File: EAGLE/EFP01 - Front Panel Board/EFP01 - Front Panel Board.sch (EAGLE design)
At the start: 109 parts, among them J20 Intel EDISON, J21 PWRBUTTON, J22 SERIAL CONS., J23 B14B-PH, J3 USB-A, J4 101-00581-59, J9 ESTOP, Q2 25MHz, U10 FT231XS-R, U11 74LVC1T45, U12 74LVC1T45, U13 74LVC1T45, U14 74LVC1T45, U15 74LVC1T45, U16 TXS0206-29, U17 74LVC, U18 MIC2026-1YM, U19 MIC2026-1YM, U20 74LVC, U21 74LVC1T45, U22 74LVC1T45, U3 93LC66A, U4 LAN9514, U9 SP3485

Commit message: Finalized schematics (minus potential LDO regulator) for all boards. Layout partially done for EFD01
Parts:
- removed C36: 220uF, TinWhiskers:CPL-CAP-ALU-SMD-220-50V
- removed C50: 470uF, TinWhiskers:CPL-CAP-ALU-SMD-470UF-25V
- removed FID4, FID5, FID6: FIDUCIAL, FirePick:FIDUCIAL
- removed J21: PWRBUTTON, TinWhiskers:CPL-CON-HEADER-0.1IN-2P-M
- removed J22: SERIAL CONS., TinWhiskers:CPL-CON-HEADER-0.1IN-4P-M
- removed J23: B14B-PH, TinWhiskers:CPL-CON-JST-2.0MM-14P-M-VRT
- removed J9: ESTOP, TinWhiskers:CPL-CON-HEADER-0.1IN-2P-M
- removed L2: 100uH, TinWhiskers:CPL-IND-100UH-1.8A
- added C1: 220uF, TinWhiskers:CPL-CAP-ALU-SMD-220UF-16V
- added C3: 470uF, TinWhiskers:CPL-CAP-ALU-SMD-470UF-10V
- added J1: PWRBTN, TinWhiskers:CPL-CON-JST-2.0MM-4P-M-SMT-RA
- added J16, J17, J6: S8B-PH-SM4, TinWhiskers:CPL-CON-JST-2.0MM-8P-M-RA
- added J18: S6B-PH-SM4, TinWhiskers:CPL-CON-JST-2.0MM-6P-M-RA
- added J2: ESTOP, TinWhiskers:CPL-CON-JST-2.0MM-2P-M-SMT-RA
- added J5: LCD, TinWhiskers:CPL-CON-HEADER-0.1IN-17P2-M
- added J7: USB-B, TinWhiskers:CPL-CON-USB-B-SMT-VERT
- added L1: 100uH, TinWhiskers:CPL-IND-100UH-700MA-2020
- added R1: 4.7K, TinWhiskers:CPL-RES-0603-4.7K-0.1W
- added R2: 10K, TinWhiskers:CPL-RES-0603-10K-0.1W
- added R3: ORNG, TinWhiskers:CPL-RES-0603-0-0.1W
- added TB1: DCIN, TinWhiskers:CPL-TBLK-SCR-3CKT-5.0MM-OST
- added U1, U2, U23, U24, U25, U26, U27, U28, U30, U5, U6, U7, U8: 74LVC1T45, TinWhiskers:CPL-TRS-74LVC1T45
- J3: value USB-A -> USB-A(2.0); device TinWhiskers:CPL-CON-HEADER-0.1IN-4P-M -> TinWhiskers:CPL-CON-USB-A-THRU-VERT-2.0; PARTNO 68000-104HLF -> (none)
- U17, U20: value 74LVC -> OR
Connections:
- removed net ESTOP_OE: J9.2
- new net !ENBL_MOD: J16.2, J17.2, J18.2, J6.2
- new net +24V: J16.1, J17.1, J18.1, J6.1, R3.2, TB1.1
- new net 74DIR: J20.GP165, U30.3
- new net 74DIRO: U1.5, U2.5, U23.5, U24.5, U25.5, U26.5, U27.5, U28.5, U30.4, U5.5, U6.5, U7.5, U8.5
- new net D0O: J20.GP40, U24.4
- new net D1O: J20.GP41, U23.4
- new net D2O: J20.GP42, U7.4
- new net D3O: J20.GP43, U8.4
- new net D4O: J20.GP44, U6.4
- new net D5O: J20.GP45, U5.4
- new net D6O: J20.GP46, U1.4
- new net D7O: J20.GP47, U2.4
- new net ESTOPIN: J2.1, R2.1
- new net LCD_BL: J5.23
- new net LCD_CLK: J5.34
- new net LCD_D10: J5.16
- new net LCD_D11: J5.17
- new net LCD_D12: J5.18
- new net LCD_D13: J5.19
- new net LCD_D14: J5.20
- new net LCD_D15: J5.21
- new net LCD_D8: J5.14
- new net LCD_D9: J5.15
- new net LCD_FCS: J5.32
- new net LCD_MISO: J5.29
- new net LCD_MOSI: J5.30
- new net LCD_PEN: J5.31
- new net LCD_RST: J5.5
- new net LCD_SDCS: J5.22
- new net LCD_TCS: J5.33
- new net LCSO: J20.GP183, U25.4
- new net LRDO: J20.GP182, U27.4
- new net LRSO: J20.GP49, U28.4
- new net LWRO: J20.GP48, U26.4
- new net N$10: J2.2, R1.2
- new net NC: J5.28
- new net VDD: J5.24, J5.25
- net !PWRBTN: now also J1.1; no longer J21.1
- net +1V8: now also U1.1, U2.6, U23.1, U24.1, U25.6, U26.6, U27.6, U28.6, U30.6, U5.1, U6.1, U7.1, U8.6
- net +3V3: now also C3.POS, L1.2, R2.2, U1.6, U2.1, U23.6, U24.6, U25.1, U26.1, U27.1, U28.1, U30.1, U5.6, U6.6, U7.6, U8.1; no longer C50.POS, J23.1, L2.2
- net +5V: now also C1.POS, J18.6, J6.6, TB1.2; no longer C36.POS
- net A: now also J16.4, J17.4, J18.4, J6.4
- net B: now also J16.5, J17.5, J18.5, J6.5
- net DM: now also J7.3; no longer J22.3
- net DP: now also J7.2; no longer J22.2
- net EE_D+: now also J16.7
- net EE_D-: now also J16.8
- net GND: now also C1.NEG, C3.NEG, J1.2, J1.4, J16.3, J17.3, J18.3, J3.GND, J5.26, J5.27, J6.3, J7.4, R1.1, TB1.3, U1.2, U2.2, U23.2, U24.2, U25.2, U26.2, U27.2, U28.2, U30.2, U30.5, U5.2, U6.2, U7.2, U8.2; no longer C36.NEG, C50.NEG, J21.2, J22.4, J23.2, J3.4
- net LCD_CS: now also J5.1, U25.3; no longer J20.GP183, J23.11
- net LCD_D0: now also J5.6, U24.3; no longer J20.GP40, J23.3
- net LCD_D1: now also J5.7, U23.3; no longer J20.GP41, J23.4
- net LCD_D2: now also J5.8, U7.3; no longer J20.GP42, J23.5
- net LCD_D3: now also J5.9, U8.3; no longer J20.GP43, J23.6
- net LCD_D4: now also J5.10, U6.3; no longer J20.GP44, J23.7
- net LCD_D5: now also J5.11, U5.3; no longer J20.GP45, J23.8
- net LCD_D6: now also J5.12, U1.3; no longer J20.GP46, J23.9
- net LCD_D7: now also J5.13, U2.3; no longer J20.GP47, J23.10
- net LCD_RD: now also J5.4, U27.3; no longer J20.GP182, J23.14
- net LCD_RS: now also J5.2, U28.3; no longer J20.GP49, J23.12
- net LCD_WR: now also J5.3, U26.3; no longer J20.GP48, J23.13
- net N$16: now also L1.1; no longer L2.1
- net N$2: now also J7.1; no longer J22.1
- net N$5: now also J1.3, R3.1; no longer J9.1
- net PWR1: now also J16.6
- net PWR2: now also J17.6
- net PWR3: now also J3.VCC; no longer J3.1
- net ULC_D+: now also J17.7
- net ULC_D-: now also J17.8
- net USBA_D+: now also J3.D+; no longer J3.3
- net USBA_D-: now also J3.D-; no longer J3.2
- net USBMCU+: now also J6.7
- net USBMCU-: now also J6.8
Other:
- note added: "CAMERA"
- note added: "DC IN"
- note added: "EFFECTOR"
- note added: "EMC03 CONNX"
- note added: "END"
- note added: "IC PWR"
- note added: "MOD."
- note added: "TEST PADS"
- note added: "TOOL1"
- note added: "UP-LOOK"
- note added: "USB CHIP (S CONS)"
- note removed: "Change to SMD pads, bottom"
- note removed: "EMERGENCY STOP SWITCH (NORMALLY CLOSED TYPE) USE JUMPER IF NOT PRESENT"
- note removed: "LOGIC IC PWR"
- note removed: "TEST POINTS"
- note removed: "TODO: CHANGE J3 TO VERT. MOUNT USB "A" CONNECTOR"
- note removed: "TODO: Replace with 34-pin 2-row 0.1" rect."
- note removed: "USB-A CHIP (S CONS)"
- note removed: "VDD"
- note removed: "VSS"
- moved on the sheet: C13, C14, C18, C19, C2, C20, C21, C22, C23, C24, C25, C26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

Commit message: Routed all boards. EFP01 has a serious problem with spacing. Even on minimum allowable there are 300 DRC errors.
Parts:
- removed C1: 220uF, TinWhiskers:CPL-CAP-ALU-SMD-220UF-16V
- removed C33, C34, C35: 0.1uF, TinWhiskers:CPL-CAP-X5R-0603-0.1UF-35V
- removed C51: 0.47uF, TinWhiskers:CPL-CAP-X7R-0603-0.47UF-10V
- removed D15: SJPB-H6, TinWhiskers:CPL-DIO-SJPB-H6-SM2
- removed J4: 101-00581-59, TinWhiskers:CPL-CON-MICSROSD(SD)-CD
- removed L1: 100uH, TinWhiskers:CPL-IND-100UH-700MA-2020
- removed R17, R23: 10.5K, TinWhiskers:CPL-RES-0603-10.5K-0.1W
- removed U16: TXS0206-29, TinWhiskers:TXS0206-29
- removed VR2: SI-8033JD, TinWhiskers:CPL-REG-SWI-3.3V-1.5A
- added C4: 10uF, TinWhiskers:CPL-CAP-ALU-6.4MM-10UF-10V
- added VR1: LMS8117AMP-3.3/NOPB, TinWhiskers:CPL-REG-LIN-3.3V-1A
- C3: value 470uF -> 10uF; device TinWhiskers:CPL-CAP-ALU-SMD-470UF-10V -> TinWhiskers:CPL-CAP-ALU-6.4MM-10UF-10V
- J5: device TinWhiskers:CPL-CON-HEADER-0.1IN-17P2-M -> TinWhiskers:CPL-CON-LCD-HDR-0.1IN-17P2-F
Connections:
- removed net CLKA: J20.GP78, U16.CLKA
- removed net CLKB: J4.CLK, U16.CLKB
- removed net CLKF: J20.GP84, U16.CLKF
- removed net CMD: J4.CMD
- removed net CMDA: J20.GP79, U16.CMDA
- removed net CMDB: U16.CMDB
- removed net DAT0A: J20.GP80, U16.DAT0A
- removed net DAT0B: J4.DAT0, U16.DAT0B
- removed net DAT1A: J20.GP81, U16.DAT1A
- removed net DAT1B: J4.DAT1, U16.DAT1B
- removed net DAT2: J4.DAT2
- removed net DAT2A: J20.GP82, U16.DAT2A
- removed net DAT2B: U16.DAT2B
- removed net DAT3: J4.CD/DAT3
- removed net DAT3A: J20.GP83, U16.DAT3A
- removed net DAT3B: U16.DAT3B
- removed net EN: R17.1, U16.EN
- removed net N$16: D15.C, L1.1, VR2.2
- removed net N$17: C51.2, VR2.5
- removed net SD_CD: J20.GP77, J4.CD, R23.1, U16.CD
- removed net VCCB: C34.2, J4.VDD, U16.VCCB
- new net RESET: U10.!RESET
- net !RXLED: now also U10.CBUS2
- net !TXLED: now also U10.CBUS1
- net +1V8: no longer C35.2, R17.2, R23.2, U16.VCCA
- net +3V3: now also C4.POS, U10.VCCIO, VR1.OUT; no longer C3.POS, C33.2, L1.2, U16.VBATT, VR2.4
- net +5V: now also C3.POS, VR1.IN; no longer C1.POS, VR2.1
- net DM: now also U10.USBDM
- net DP: now also U10.USBDP
- net GND: now also C4.NEG, RJ1.GND, U10.GND@16, U10.GND@6, VR1.GND, VR1.TAB; no longer C1.NEG, C33.1, C34.1, C35.1, C51.1, D15.A, J4.GND, J4.GND2, J4.NC, J4.VSS, U16.GND@C2, U16.GND@C3, VR2.3, VR2.GND
- net N$1: now also U10.3V3OUT
- net RXD: now also U10.RXD
- net TXDO: now also U10.TXD
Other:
- note added: "VOLTAGE REG"
- note removed: "* 5V Switching Regulator: Powers LEDs, Endstops"
- note removed: "MICRO SD INTERFACE"
- note removed: "TODO: MAY CHANGE TO FULL-SIZE SD?"
- moved on the sheet: C3, J5

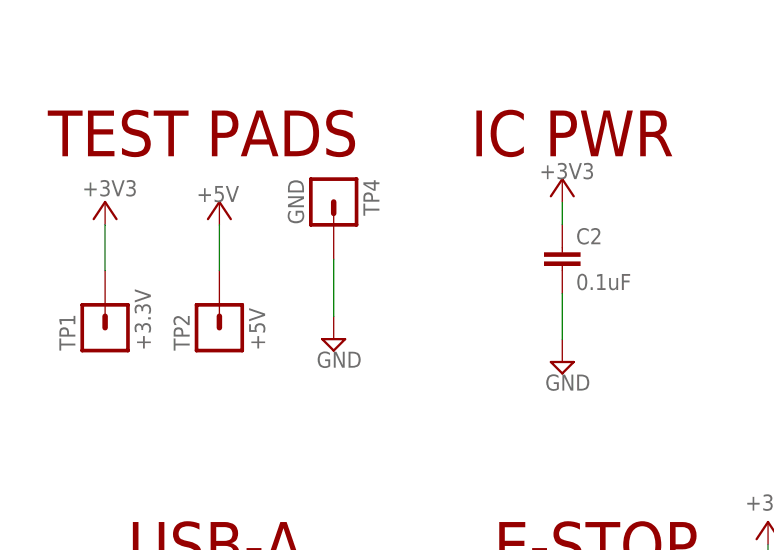
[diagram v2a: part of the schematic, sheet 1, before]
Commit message: Completed boards. Please look at airwires connecting thermal pads to GND vias. They shouldn't be present due to the vias.
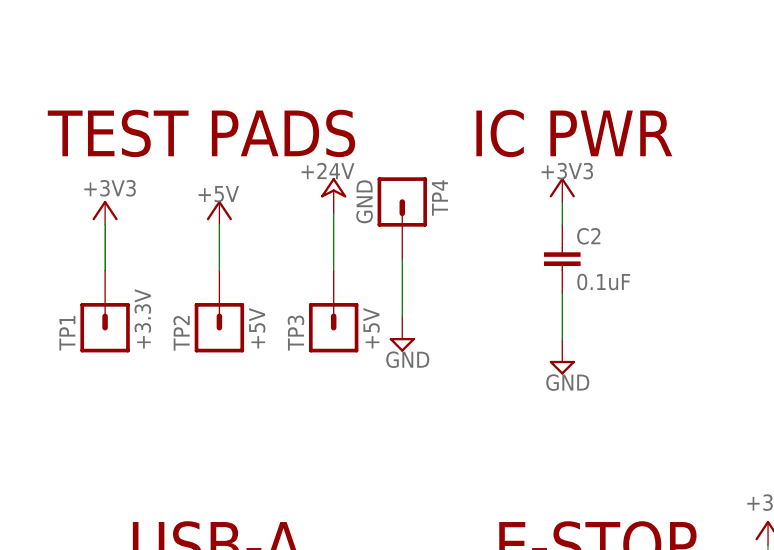
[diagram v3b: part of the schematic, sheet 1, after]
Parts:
- added TP3: +5V, TinWhiskers:TPAD
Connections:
- net +24V: now also TP3.2
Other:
- moved on the sheet: TP4
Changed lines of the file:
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@@
 <part name="+3V32" library="supply1" deviceset="+3V3" device=""/>
 <part name="SUPPLY45" library="TinWhiskers" deviceset="GND" device=""/>
+<part name="TP3" library="TinWhiskers" deviceset="TPAD" device="" value="+5V">
+<attribute name="DNP" value="T"/>
+<attribute name="PARTNO" value="N/A"/>
+</part>
+<part name="P+8" library="supply1" deviceset="+24V" device=""/>
 </parts>
 <sheets>
@@
 <instance part="SUPPLY82" gate="GND" x="243.84" y="116.84"/>
 <instance part="SUPPLY83" gate="GND" x="218.44" y="116.84"/>
-<instance part="TP4" gate="G$1" x="40.64" y="232.41" rot="R270">
-<attribute name="DNP" x="40.64" y="232.41" size="1.778" layer="96" rot="R270" display="off"/>
-<attribute name="PARTNO" x="40.64" y="232.41" size="1.778" layer="96" display="off"/>
+<instance part="TP4" gate="G$1" x="48.26" y="232.41" rot="R270">
+<attribute name="DNP" x="48.26" y="232.41" size="1.778" layer="96" rot="R270" display="off"/>
+<attribute name="PARTNO" x="48.26" y="232.41" size="1.778" layer="96" display="off"/>
 </instance>
 <instance part="TP2" gate="G$1" x="27.94" y="226.06" rot="R90">
@@
 <attribute name="VALUE" x="12.7" y="236.855" size="1.778" layer="96"/>
 </instance>
-<instance part="SUPPLY49" gate="GND" x="40.64" y="220.98"/>
+<instance part="SUPPLY49" gate="GND" x="48.26" y="220.98"/>
 <instance part="R1" gate="G$1" x="81.28" y="172.72" rot="R90"/>
 <instance part="SUPPLY3" gate="GND" x="81.28" y="162.56"/>
@@
 <instance part="+3V32" gate="G$1" x="114.3" y="81.28" smashed="yes">
 <attribute name="VALUE" x="111.76" y="81.915" size="1.778" layer="96"/>
+</instance>
+<instance part="TP3" gate="G$1" x="40.64" y="226.06" rot="R90">
+<attribute name="DNP" x="40.64" y="226.06" size="1.778" layer="96" rot="R90" display="off"/>
+<attribute name="PARTNO" x="40.64" y="226.06" size="1.778" layer="96" display="off"/>
+</instance>
+<instance part="P+8" gate="1" x="40.64" y="237.49" smashed="yes">
+<attribute name="VALUE" x="36.83" y="238.76" size="1.778" layer="96"/>
 </instance>
 </instances>
@@
 <segment>
 <pinref part="TP4" gate="G$1" pin="2"/>
-<wire x1="40.64" y1="229.87" x2="40.64" y2="223.52" width="0.1524" layer="91"/>
+<wire x1="48.26" y1="229.87" x2="48.26" y2="223.52" width="0.1524" layer="91"/>
 <pinref part="SUPPLY49" gate="GND" pin="GND"/>
 </segment>
@@
 <pinref part="P+13" gate="1" pin="+24V"/>
 </segment>
-</net>
+<segment>
+<pinref part="TP3" gate="G$1" pin="2"/>
+<wire x1="40.64" y1="228.6" x2="40.64" y2="234.95" width="0.1524" layer="91"/>
+<pinref part="P+8" gate="1" pin="+24V"/>
+</segment>
+</net>

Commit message: Updated all boards to include changes for production
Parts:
- added C1, C10, C15, C16, C17, C27, C28, C29, C33, C34, C35, C36, C37, C38, C39, C40, C41, C42, C43, C44, C45, C46, C47, C48, C49, C5, C6, C7, C8, C9: 0.1uF, TinWhiskers:CPL-CAP-X5R-0603-0.1UF-35V
- added LOGO1, LOGO2: LOGO-FIREPICKLARGE, FirePick:LOGO-FIREPICKLARGE
- J16, J17, J6: device TinWhiskers:CPL-CON-JST-2.0MM-8P-M-RA -> TinWhiskers:CPL-CON-JST-2.0MM-8P-SMT-VRT
- J18: device TinWhiskers:CPL-CON-JST-2.0MM-6P-M-RA -> TinWhiskers:CPL-CON-JST-2.0MM-6P-SMT-VRT
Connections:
- net +3V3: now also C1.2, C10.2, C15.2, C16.2, C17.2, C27.2, C28.2, C29.2, C33.2, C34.2, C35.2, C36.2, C37.2, C38.2, C39.2, C40.2, C41.2, C42.2, C43.2, C44.2, C45.2, C46.2, C47.2, C48.2, C49.2, C5.2, C6.2, C7.2, C8.2, C9.2, VR1.TAB; no longer VR1.OUT
- net GND: now also C1.1, C10.1, C15.1, C16.1, C17.1, C27.1, C28.1, C29.1, C33.1, C34.1, C35.1, C36.1, C37.1, C38.1, C39.1, C40.1, C41.1, C42.1, C43.1, C44.1, C45.1, C46.1, C47.1, C48.1, C49.1, C5.1, C6.1, C7.1, C8.1, C9.1; no longer VR1.TAB
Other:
- moved on the sheet: C3, C4, C60, C61, C78, FB3, J7, VR1

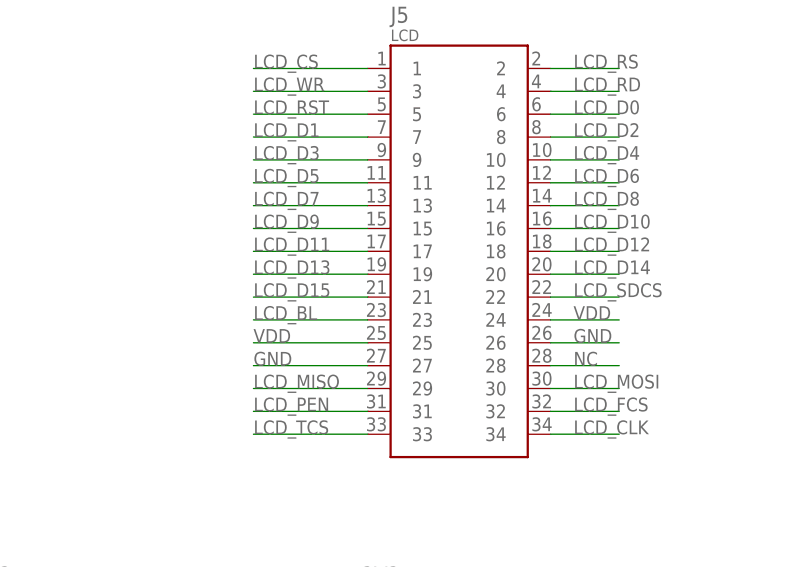
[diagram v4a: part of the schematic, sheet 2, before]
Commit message: Added +3V3 line for LCD, DXF for Will
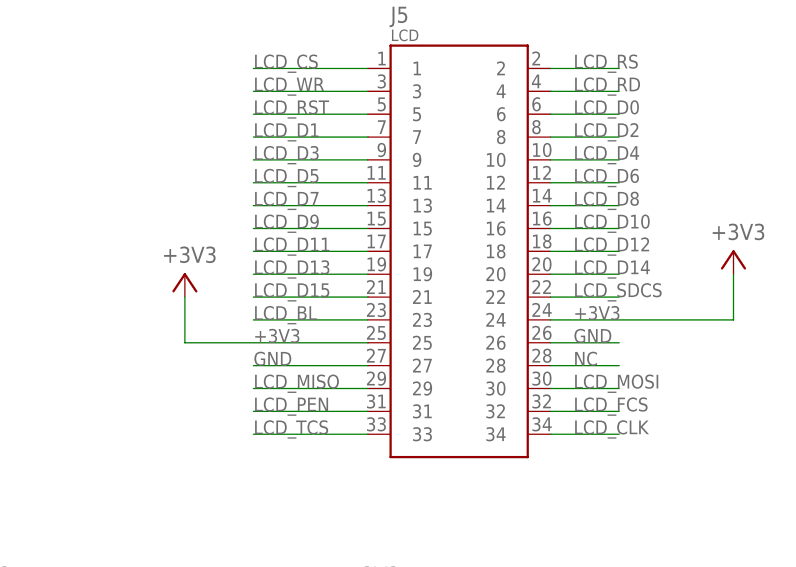
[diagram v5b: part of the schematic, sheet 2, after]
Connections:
- removed net VDD: J5.24, J5.25
- net +3V3: now also J5.24, J5.25
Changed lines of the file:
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@@
 <part name="SUPPLY104" library="TinWhiskers" deviceset="GND" device=""/>
 <part name="SUPPLY105" library="TinWhiskers" deviceset="GND" device=""/>
+<part name="+3V64" library="supply1" deviceset="+3V3" device=""/>
+<part name="+3V65" library="supply1" deviceset="+3V3" device=""/>
 </parts>
 <sheets>
@@
 <instance part="SUPPLY45" gate="GND" x="287.02" y="162.56"/>
 <instance part="LOGO2" gate="G$1" x="86.36" y="10.16"/>
+<instance part="+3V64" gate="G$1" x="317.5" y="109.22" smashed="yes">
+<attribute name="VALUE" x="314.96" y="110.49" size="1.778" layer="96"/>
+</instance>
+<instance part="+3V65" gate="G$1" x="378.46" y="111.76" smashed="yes">
+<attribute name="VALUE" x="375.92" y="113.03" size="1.778" layer="96"/>
+</instance>
 </instances>
 <busses>
@@
 <pinref part="+3V33" gate="G$1" pin="+3V3"/>
 </segment>
+<segment>
+<pinref part="J5" gate="G$1" pin="24"/>
+<label x="360.68" y="104.14" size="1.524" layer="95"/>
+<pinref part="+3V65" gate="G$1" pin="+3V3"/>
+<wire x1="358.14" y1="104.14" x2="378.46" y2="104.14" width="0.1524" layer="91"/>
+<wire x1="378.46" y1="104.14" x2="378.46" y2="109.22" width="0.1524" layer="91"/>
+</segment>
+<segment>
+<pinref part="J5" gate="G$1" pin="25"/>
+<wire x1="337.82" y1="101.6" x2="317.5" y2="101.6" width="0.1524" layer="91"/>
+<label x="325.12" y="101.6" size="1.524" layer="95"/>
+<pinref part="+3V64" gate="G$1" pin="+3V3"/>
+<wire x1="317.5" y1="101.6" x2="317.5" y2="106.68" width="0.1524" layer="91"/>
+</segment>
 </net>
 <net name="N$7" class="0">
@@
 </segment>
 </net>
-<net name="VDD" class="0">
-<segment>
-<pinref part="J5" gate="G$1" pin="25"/>
-<wire x1="337.82" y1="101.6" x2="325.12" y2="101.6" width="0.1524" layer="91"/>
-<label x="325.12" y="101.6" size="1.524" layer="95"/>
-</segment>
-<segment>
-<pinref part="J5" gate="G$1" pin="24"/>
-<wire x1="365.76" y1="104.14" x2="358.14" y2="104.14" width="0.1524" layer="91"/>
-<label x="360.68" y="104.14" size="1.524" layer="95"/>
-</segment>
-</net>

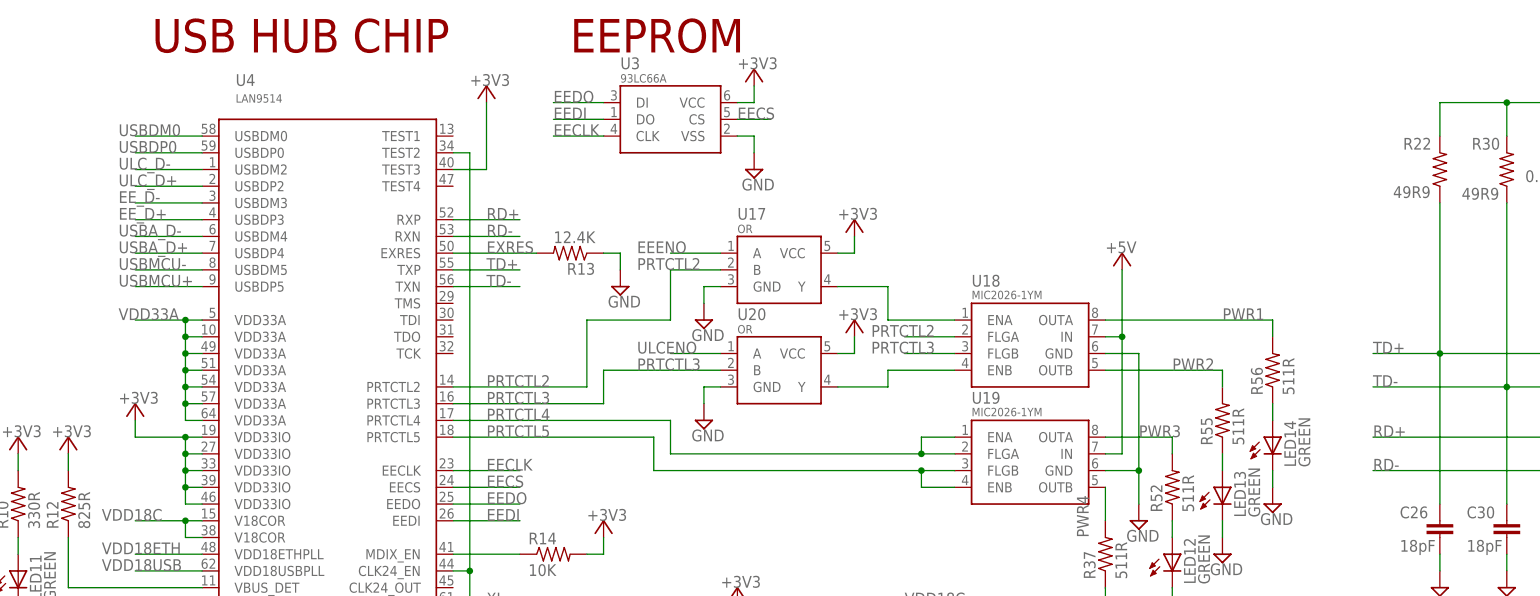
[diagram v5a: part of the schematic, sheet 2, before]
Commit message: Partially-routed diff pairs
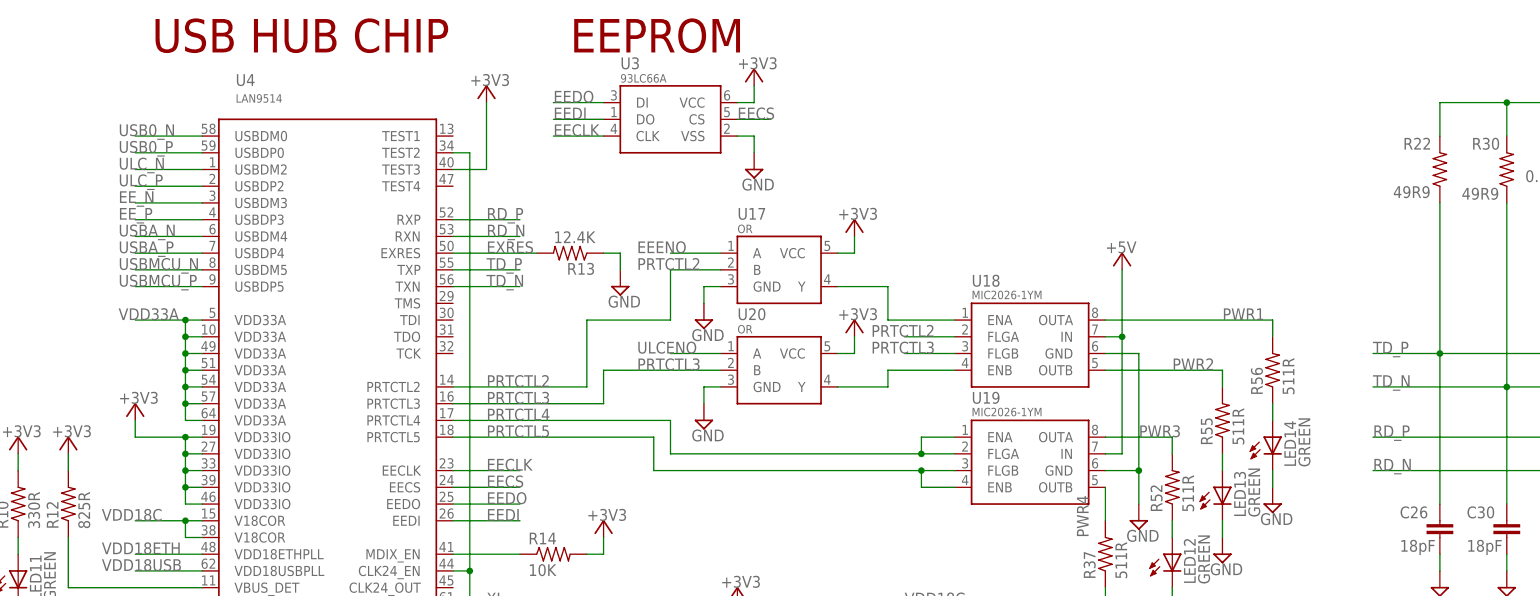
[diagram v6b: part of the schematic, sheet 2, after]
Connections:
- net EE_D+ renamed EE_P
- net EE_D- renamed EE_N
- net RD+ renamed RD_P
- net RD- renamed RD_N
- net TD+ renamed TD_P
- net TD- renamed TD_N
- net ULC_D+ renamed ULC_P
- net ULC_D- renamed ULC_N
- net USBA_D+ renamed USBA_P
- net USBA_D- renamed USBA_N
- net USBDM0 renamed USB0_N
- net USBDP0 renamed USB0_P
- net USBMCU+ renamed USBMCU_P
- net USBMCU- renamed USBMCU_N
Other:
- note removed: "(10-PIN JST PH SERIES)"
- note removed: "TODO: ADD CONNECTOR FOR USBs TO EMC03"
- note removed: "TODO: ADD INCOMING +6VDC POWER CONNECTOR"
- note removed: "TODO: CHANGE J22 TO USB "B" VERT. MOUNT"
